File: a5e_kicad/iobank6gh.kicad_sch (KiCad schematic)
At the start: 1 part, among them U7 A5EB013B-B23B

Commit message: Schematic reorg step 1: remove dangling stubs and stale notes, correct notes, fill title blocks
Netlist: 0 renamed, 0 connectivity diffs; DRC parity 0. ERC 315 -> 242.
Plan refreshed for the eMMC, RTL8211FDI, TPS548A28 and the tuned LPDDR4 (IOBANK 3 sheet name kept).
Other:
- note added: "VCCIO_6G : 3V3"
- note removed: "VCCIO_6G : 1V8"
- title: (none) -> Banks 6G / 6H HVIO
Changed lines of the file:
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@@
 	(paper "A4")
 	(title_block
-		(rev "0.1")
+		(title "Banks 6G / 6H HVIO")
+		(rev "${REVISION}")
+		(comment 1 "${BOARD}")
 	)
-	(text "VCCIO_6G : 1V8"
+	(text "VCCIO_6G : 3V3"
 		(exclude_from_sim no)
 		(at 165.1 22.86 0)

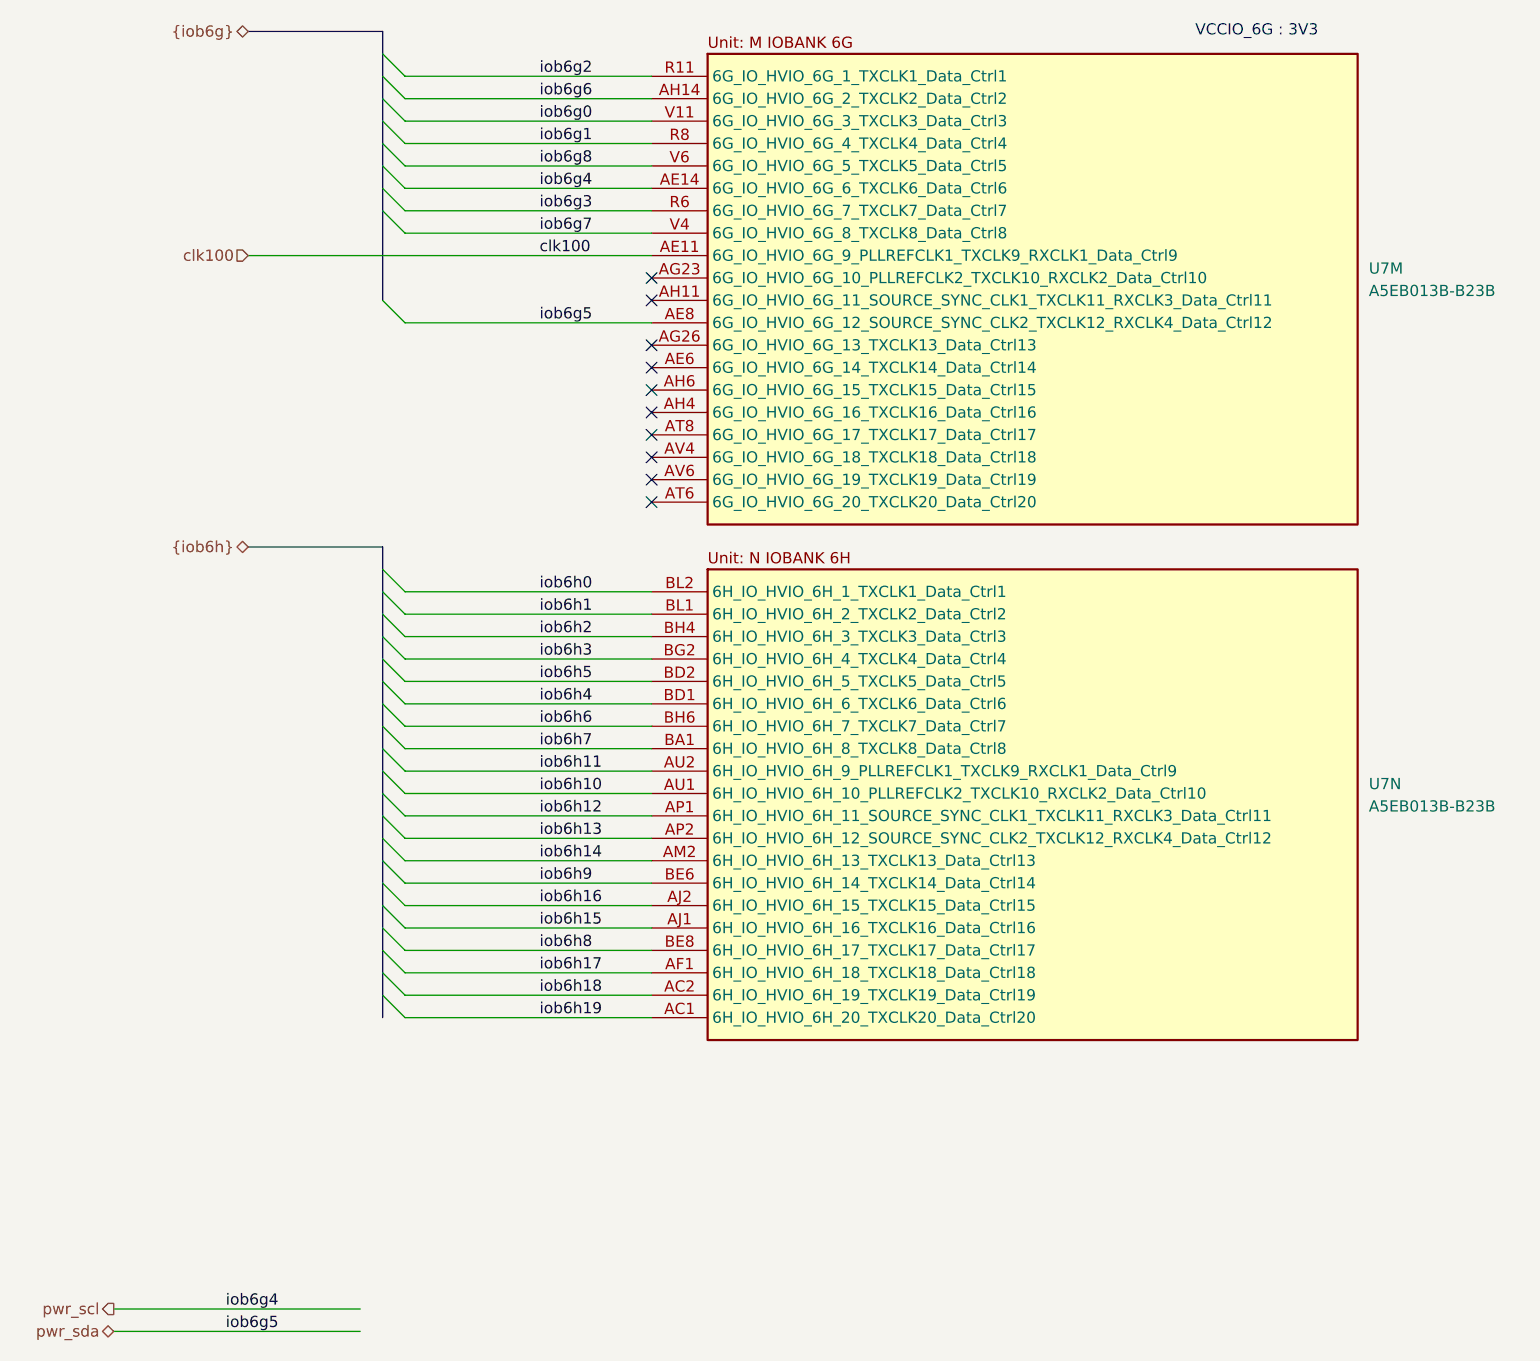
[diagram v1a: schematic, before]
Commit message: Schematic reorg step 7: no global labels, NC flags on unused U7 pins
- hps_uart0_tx/rx, eth_rst_n, phy_rst_n, fpga_led: global labels replaced by
  sheet pins; eth_led_g_n is a local label
- HyperBus labels/bus, the HPS {hps_i2c} bus and the pwr_scl/pwr_sda wiring
  removed (nothing behind them)
- 118 U7 pins that only had a net label: label, stub and bus entry removed,
  no-connect flag added
- Bank 3A notes restacked
- PCB: 124 nets renamed (118 to unconnected-(U7...))

Netdiff: 124 renamed, 0 connectivity diffs. ERC 148 -> 21. DRC parity 0.
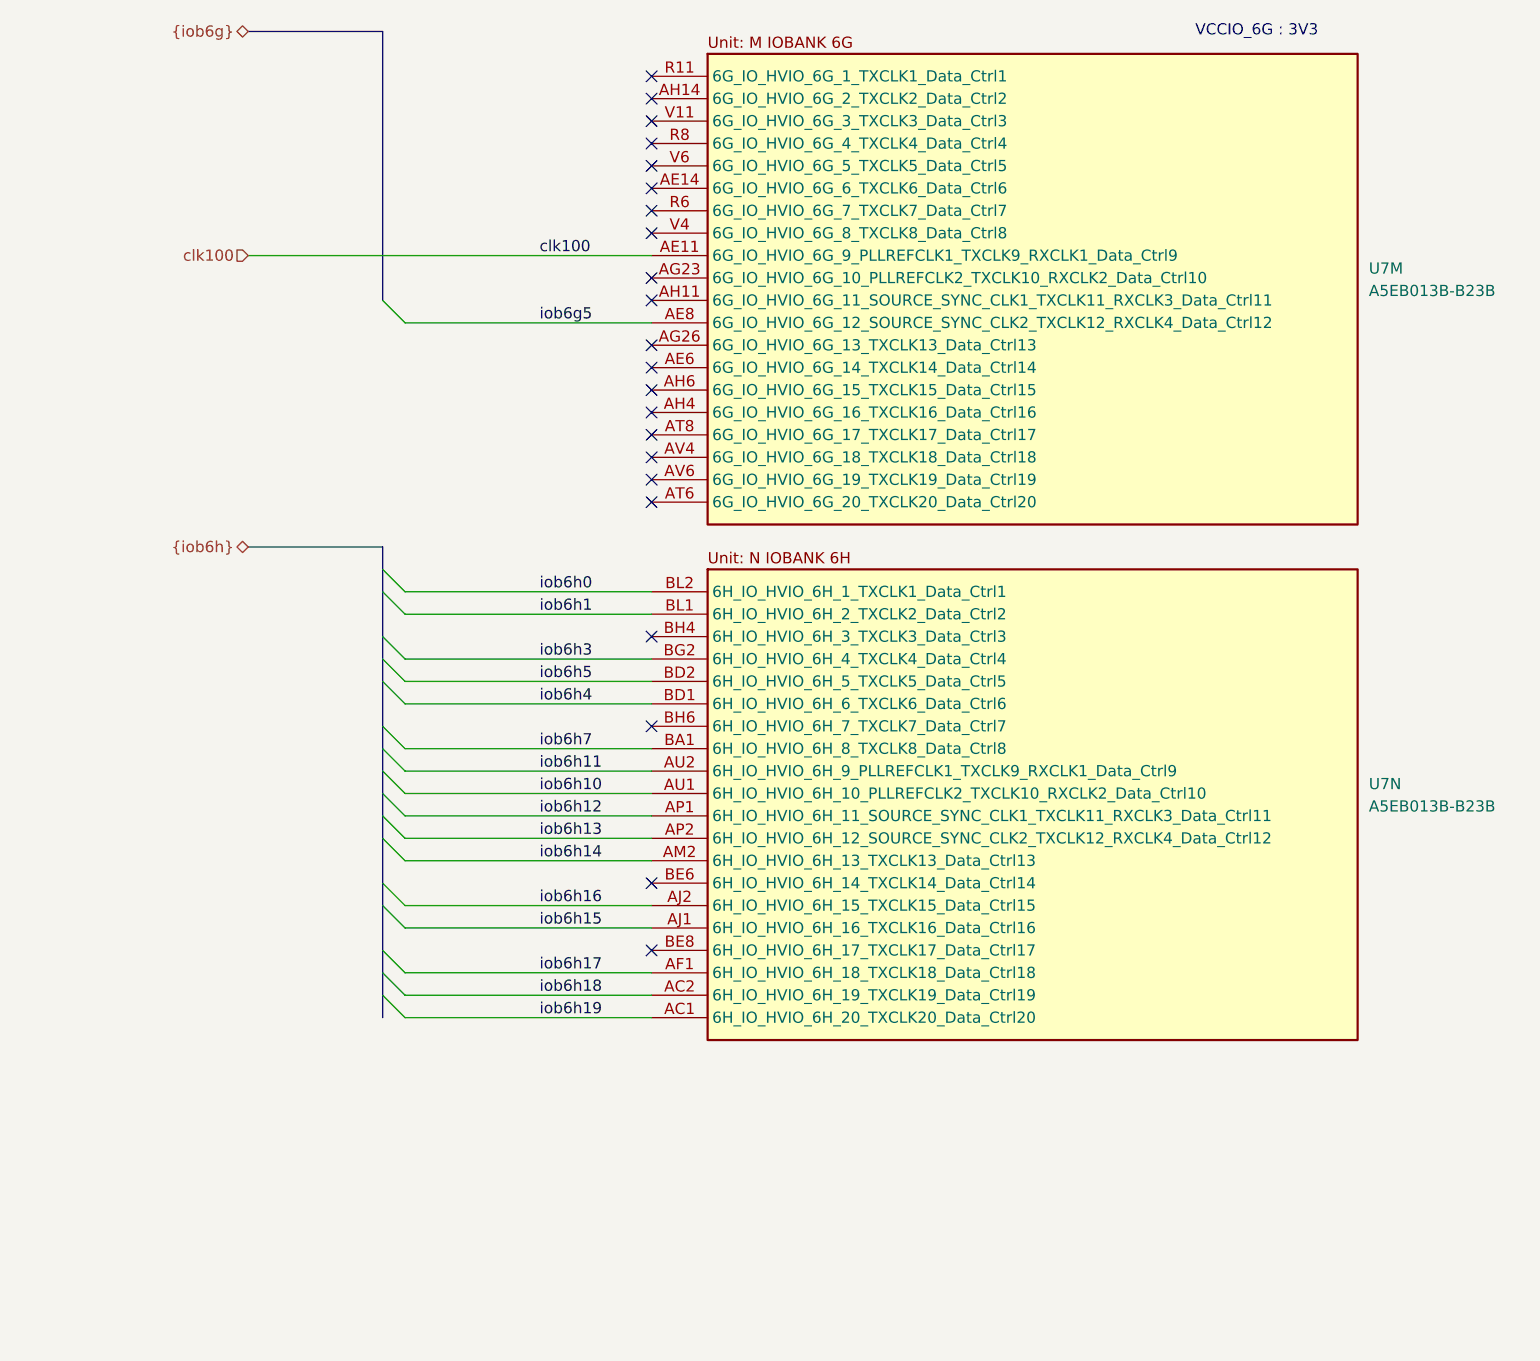
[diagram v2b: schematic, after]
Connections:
- net iob6g0: no longer names the net of U7.V11 (6G_IO_HVIO_6G_3_TXCLK3_Data_Ctrl3)
- net iob6g1: no longer names the net of U7.R8 (6G_IO_HVIO_6G_4_TXCLK4_Data_Ctrl4)
- net iob6g2: no longer names the net of U7.R11 (6G_IO_HVIO_6G_1_TXCLK1_Data_Ctrl1)
- net iob6g3: no longer names the net of U7.R6 (6G_IO_HVIO_6G_7_TXCLK7_Data_Ctrl7)
- net iob6g6: no longer names the net of U7.AH14 (6G_IO_HVIO_6G_2_TXCLK2_Data_Ctrl2)
- net iob6g7: no longer names the net of U7.V4 (6G_IO_HVIO_6G_8_TXCLK8_Data_Ctrl8)
- net iob6g8: no longer names the net of U7.V6 (6G_IO_HVIO_6G_5_TXCLK5_Data_Ctrl5)
- net iob6h2: no longer names the net of U7.BH4 (6H_IO_HVIO_6H_3_TXCLK3_Data_Ctrl3)
- net iob6h6: no longer names the net of U7.BH6 (6H_IO_HVIO_6H_7_TXCLK7_Data_Ctrl7)
- net iob6h8: no longer names the net of U7.BE8 (6H_IO_HVIO_6H_17_TXCLK17_Data_Ctrl17)
- net iob6h9: no longer names the net of U7.BE6 (6H_IO_HVIO_6H_14_TXCLK14_Data_Ctrl14)
- net pwr_scl: no longer names the net of U7.AE14 (6G_IO_HVIO_6G_6_TXCLK6_Data_Ctrl6)
- net pwr_sda renamed iob6g5
- no-connect marks 10 -> 22
